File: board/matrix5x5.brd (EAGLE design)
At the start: 100 x 90 mm, 26 parts

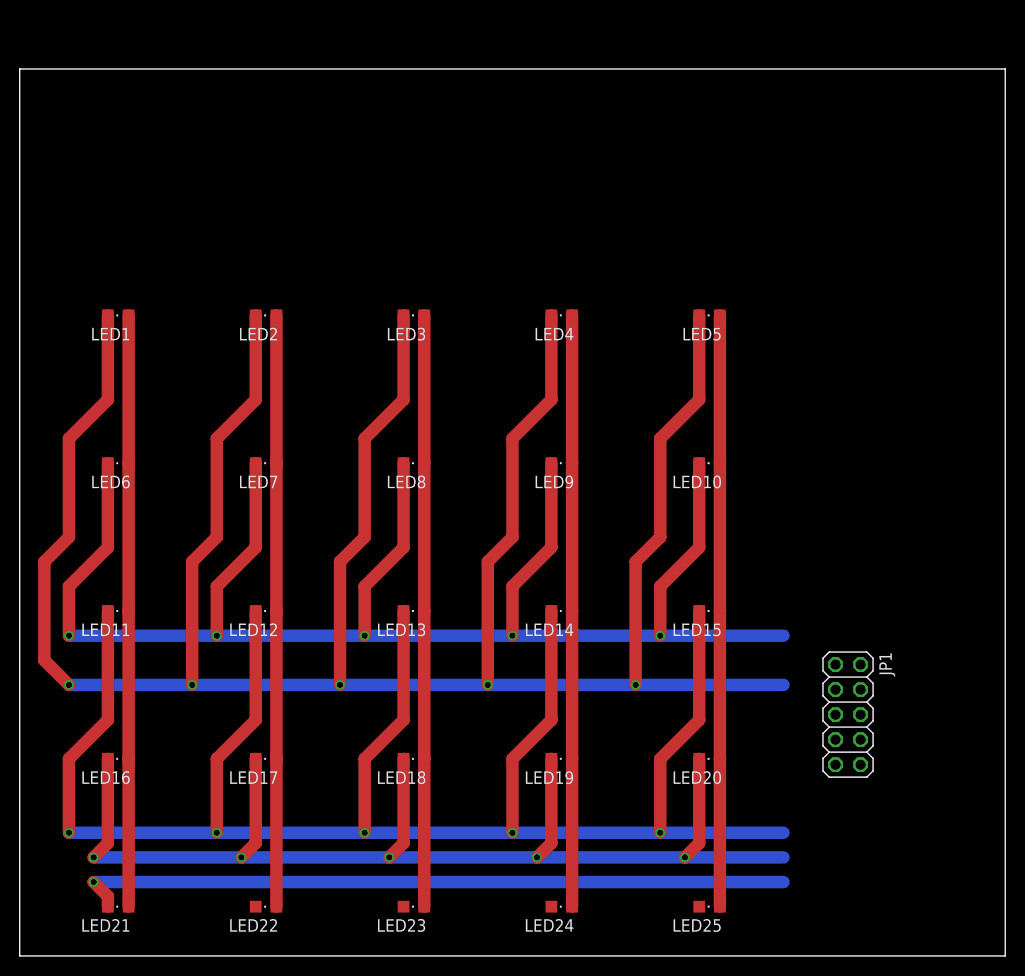
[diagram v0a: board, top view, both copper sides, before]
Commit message: board: fix net name and add artwork
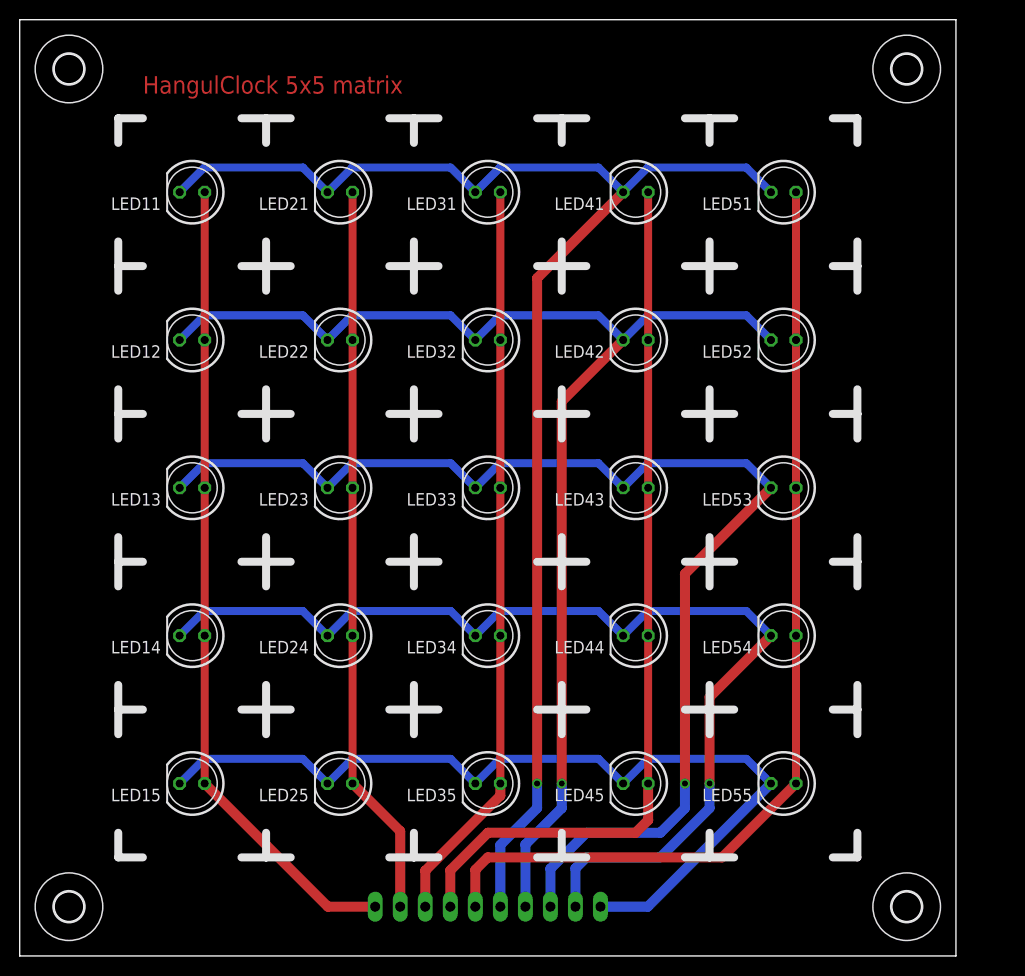
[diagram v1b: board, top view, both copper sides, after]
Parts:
- removed LED1, LED10, LED16, LED17, LED18, LED19, LED2, LED20, LED3, LED4, LED5, LED6, LED7, LED8, LED9: (no value), led:CHIPLED_0805
- added LED31, LED32, LED33, LED34, LED35, LED41, LED42, LED43, LED44, LED45, LED51, LED52, LED53, LED54, LED55: (no value), led:LED5MM
- added U$1, U$2, U$3, U$4: (no value), holes:3,0
- JP1: device pinhead:2X05 -> pinhead:1X10
- LED11, LED12, LED13, LED14, LED15, LED21, LED22, LED23, LED24, LED25: device led:CHIPLED_0805 -> led:LED5MM
- moved LED21 75.9 mm to (32.5, 77.5), turned to 180 degrees
- moved LED22 58.0 mm to (32.5, 62.5), turned to 180 degrees
- moved LED15 55.3 mm to (17.5, 17.5), turned to 180 degrees
- moved LED11 43.2 mm to (17.5, 77.5), turned to 180 degrees
- moved LED23 43.2 mm to (32.5, 47.5), turned to 180 degrees
- moved JP1 41.4 mm to (47.5, 5.00), flipped to the bottom, turned to 180 degrees
- moved LED25 39.5 mm to (32.5, 17.5), turned to 180 degrees
- moved LED14 37.6 mm to (17.5, 32.5), turned to 180 degrees
- moved LED24 35.5 mm to (32.5, 32.5), turned to 180 degrees
- moved LED12 28.5 mm to (17.5, 62.5), turned to 180 degrees
- moved LED13 25.7 mm to (17.5, 47.5), turned to 180 degrees
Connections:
- net A1: now also LED12.A, LED13.A, LED14.A, LED15.A; no longer LED1.A, LED16.A, LED21.A, LED6.A
- net A2: now also JP1.2, LED21.A, LED23.A, LED24.A, LED25.A; no longer JP1.3, LED12.A, LED17.A, LED2.A, LED7.A
- net A3: now also JP1.3, LED31.A, LED32.A, LED33.A, LED34.A, LED35.A; no longer JP1.5, LED13.A, LED18.A, LED23.A, LED3.A, LED8.A
- net A4: now also JP1.4, LED41.A, LED42.A, LED43.A, LED44.A, LED45.A; no longer JP1.7, LED14.A, LED19.A, LED24.A, LED4.A, LED9.A
- net A5: now also JP1.5, LED51.A, LED52.A, LED53.A, LED54.A, LED55.A; no longer JP1.9, LED10.A, LED15.A, LED20.A, LED25.A, LED5.A
- net K1: now also JP1.6, LED11.K, LED21.K, LED31.K, LED41.K, LED51.K; no longer JP1.2, LED1.C, LED2.C, LED3.C, LED4.C, LED5.C
- net K2: now also JP1.7, LED12.K, LED22.K, LED32.K, LED42.K, LED52.K; no longer JP1.4, LED10.C, LED6.C, LED7.C, LED8.C, LED9.C
- net K3: now also JP1.8, LED13.K, LED23.K, LED33.K, LED43.K, LED53.K; no longer JP1.6, LED11.C, LED12.C, LED13.C, LED14.C, LED15.C
- net K4: now also JP1.9, LED14.K, LED24.K, LED34.K, LED44.K, LED54.K; no longer JP1.8, LED16.C, LED17.C, LED18.C, LED19.C, LED20.C
- net K5: now also LED15.K, LED25.K, LED35.K, LED45.K, LED55.K; no longer LED21.C, LED22.C, LED23.C, LED24.C, LED25.C
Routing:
- net K1: track 274.4 -> 145.9 mm, vias 5 -> 1
- net K3: track 193.2 -> 124.4 mm, vias 5 -> 1
- net A5: track 60.0 -> 99.9 mm
- net K2: track 168.2 -> 129.9 mm, vias 5 -> 1
- net A4: track 60.0 -> 89.6 mm
- net A1: track 60.0 -> 82.5 mm
- net K5: track 73.1 -> 90.8 mm, vias 1 -> 0
- net A3: track 60.0 -> 75.7 mm
- net K4: track 123.0 -> 108.4 mm, vias 5 -> 1
- net A2: track 60.0 -> 74.5 mm
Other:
- board size 100 x 90 mm -> 95 x 95 mm
- board text added: "HangulClock 5x5 matrix"

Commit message: board: add more holes to matrix board
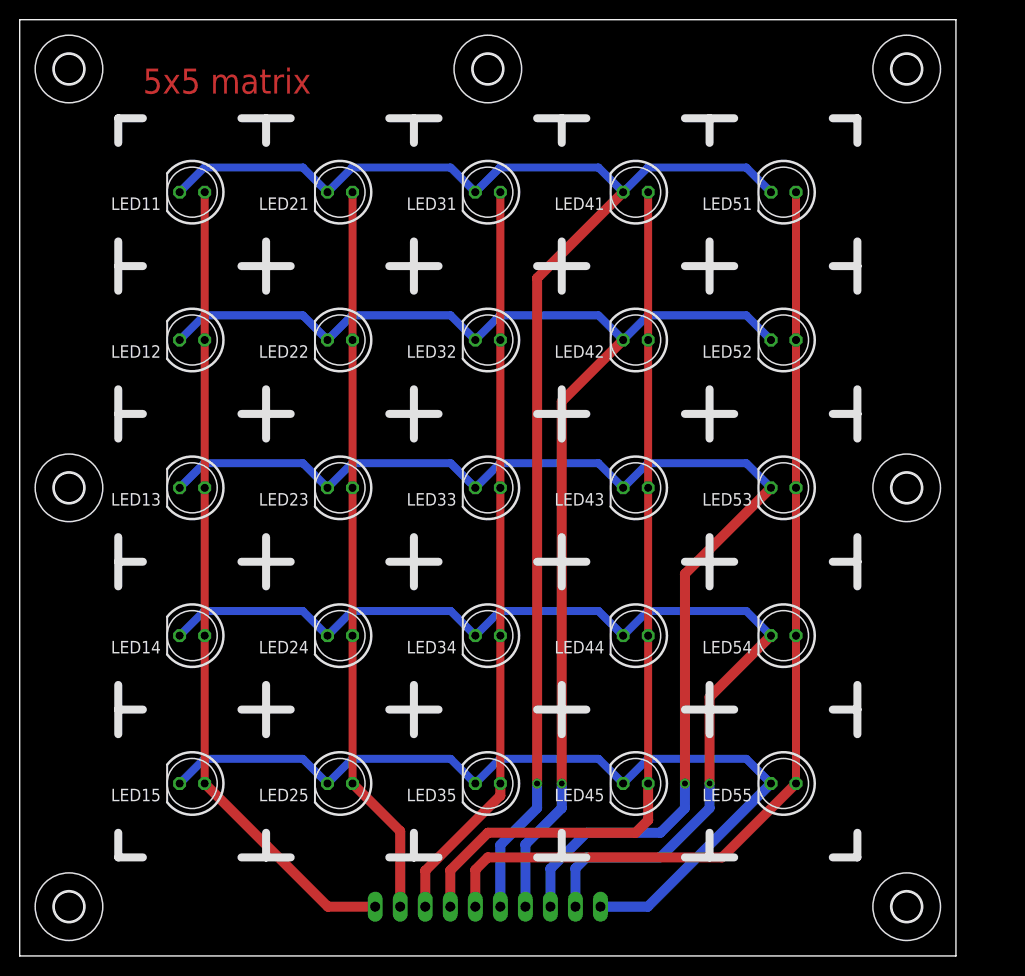
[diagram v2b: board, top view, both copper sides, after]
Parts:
- added U$5, U$6, U$7: (no value), holes:3,0
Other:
- board text added: "5x5 matrix"
- board text removed: "HangulClock 5x5 matrix"
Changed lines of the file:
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@@
 <wire x1="12.5" y1="85" x2="10" y2="85" width="0.8128" layer="21"/>
 <wire x1="10" y1="85" x2="10" y2="82.5" width="0.8128" layer="21"/>
-<text x="12.5" y="87.5" size="1.778" layer="1" font="vector">HangulClock 5x5 matrix</text>
+<text x="12.5" y="87.5" size="2.54" layer="1" font="vector">5x5 matrix</text>
 </plain>
 <attributes>
@@
 <element name="U$4" library="holes" package="3,0" value="" x="90" y="5"/>
 <element name="JP1" library="pinhead" package="1X10" value="" x="47.5" y="5" rot="MR180"/>
+<element name="U$5" library="holes" package="3,0" value="" x="47.5" y="90"/>
+<element name="U$6" library="holes" package="3,0" value="" x="5" y="47.5"/>
+<element name="U$7" library="holes" package="3,0" value="" x="90" y="47.5"/>
 </elements>
 <signals>
